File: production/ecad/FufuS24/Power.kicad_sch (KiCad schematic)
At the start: 45 parts, among them U5 TPSM365R15RDNR, U6 PLMR38020FDDAR, U7 PLMR38020FDDAR

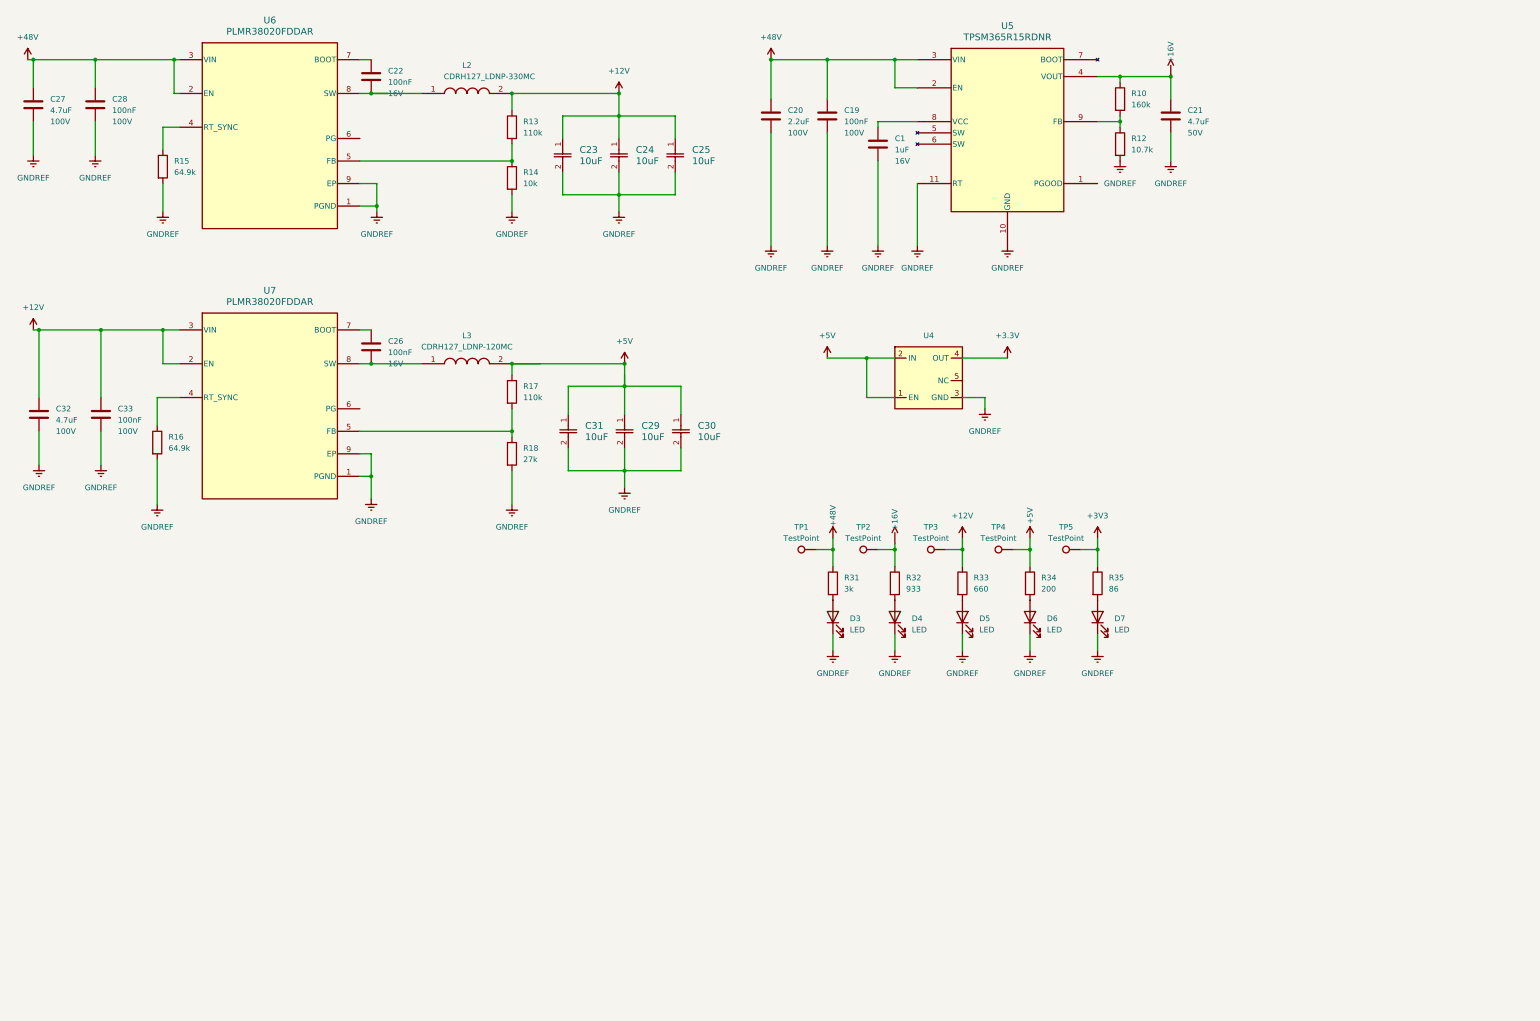
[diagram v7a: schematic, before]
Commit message: Incorporated schematic review feedback
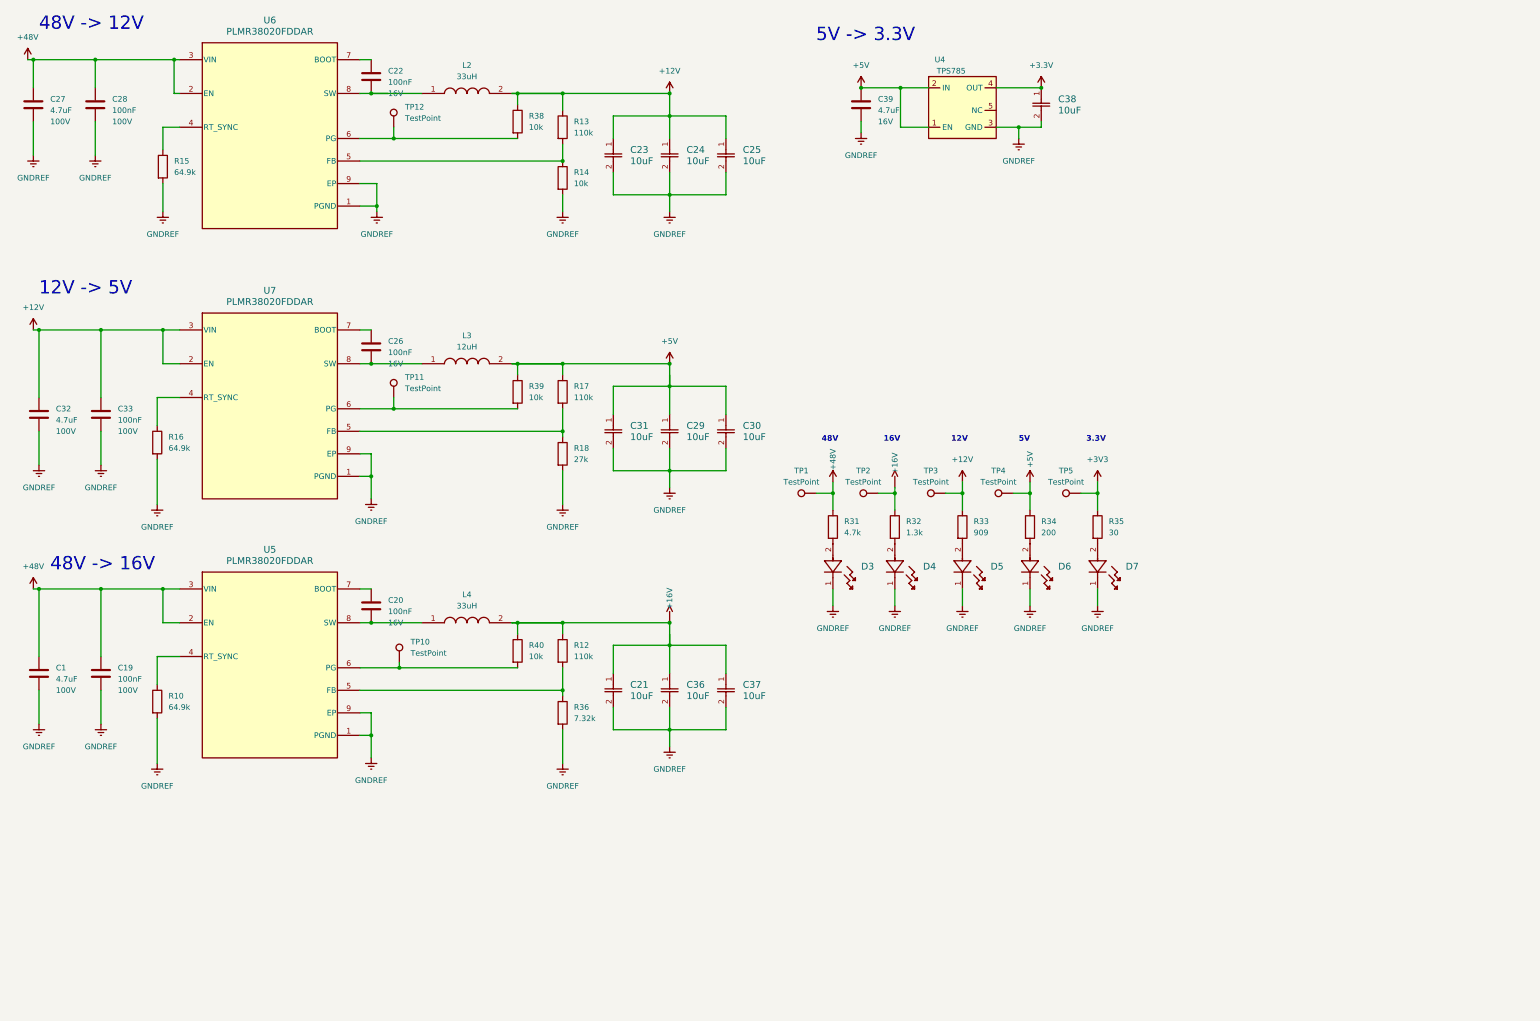
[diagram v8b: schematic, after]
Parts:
- removed C21: 4.7uF, symbol Device:C
- removed D3, D4, D5, D6, D7: LED, symbol Device:LED
- removed U5: TPSM365R15RDNR, footprints:QFN-FCMOD_365R6FRDN_TEX, symbol TPSM365R15RDNR:TPSM365R15RDNR
- added C21, C36, C37, C38: 10uF, symbol CL21A106KAYNNNG:CL21A106KAYNNNG
- added C39: 4.7uF, symbol Device:C
- added D3, D4, D5, D6, D7: 150080GS75000, LED_GS75000_WRE, symbol 150080GS75000:150080GS75000
- added L4: 33uH, footprints:INDPM120120X800N, symbol CDRH127_LDNP-330MC:CDRH127_LDNP-330MC
- added R36: 7.32k, symbol Device:R
- added R38, R39, R40: 10k, symbol Device:R
- added TP10, TP11, TP12: TestPoint, TestPoint:TestPoint_Pad_2.0x2.0mm, symbol Connector:TestPoint
- added U5: PLMR38020FDDAR, footprints:DDA0008E-MFG, symbol LMR38020FDDAR:PLMR38020FDDAR
- C1: value 1uF -> 4.7uF; Voltage 16V -> 100V
- C20: value 2.2uF -> 100nF; Voltage 100V -> 16V
- L2: value CDRH127_LDNP-330MC -> 33uH
- L3: value CDRH127_LDNP-120MC -> 12uH
- R10: value 160k -> 64.9k
- R12: value 10.7k -> 110k
- R31: value 3k -> 4.7k
- R32: value 933 -> 1.3k
- R33: value 660 -> 909
- R35: value 86 -> 30
- U4: value ~ -> TPS785
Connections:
- net +12V: now also R38.1
- net +16V: now also R12.1, C21.1, C36.1, C37.1, L4.2, R40.1; no longer R10.1
- net +3.3V: now also C38.1
- net +48V: now also C1.1, U5.2 (EN), U5.3 (VIN); no longer C20.1
- net +5V: now also C39.1, R39.1
- net GNDREF: now also R10.2, C21.2, C36.2, C37.2, C38.2, C39.2, D3.1, D4.1, D5.1, D6.1, D7.1, R36.2, U5.1 (PGND), U5.9 (EP); no longer C20.2, R12.2
- net at R32.2: now also D4.2
- net at R35.2: now also D7.2
- net at R31.2: now also D3.2
- net at R33.2: now also D5.2
- net at U7.6 (PG): now also R39.2, TP11.1
- net at R34.2: now also D6.2
- net at U6.6 (PG): now also R38.2, TP12.1
- new net: C20.1, U5.7 (BOOT)
- new net: C20.2, L4.1, U5.8 (SW)
- new net: R12.2, R36.1, U5.5 (FB)
- new net: R10.1, U5.4 (RT_SYNC)
- new net: R40.2, TP10.1, U5.6 (PG)
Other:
- note added: "12V"
- note added: "12V -> 5V"
- note added: "16V"
- note added: "3.3V"
- note added: "48V"
- note added: "48V -> 12V"
- note added: "48V -> 16V"
- note added: "5V"
- note added: "5V -> 3.3V"
- moved on the sheet: C23, C24, C25, C29, C30, C31, R13, R14, R17, R18, R31, R32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
